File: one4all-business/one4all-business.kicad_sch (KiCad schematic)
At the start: 33 parts, among them J10 T1-4, J11 TN1-4, J12 T5-8, J13 TN5-8

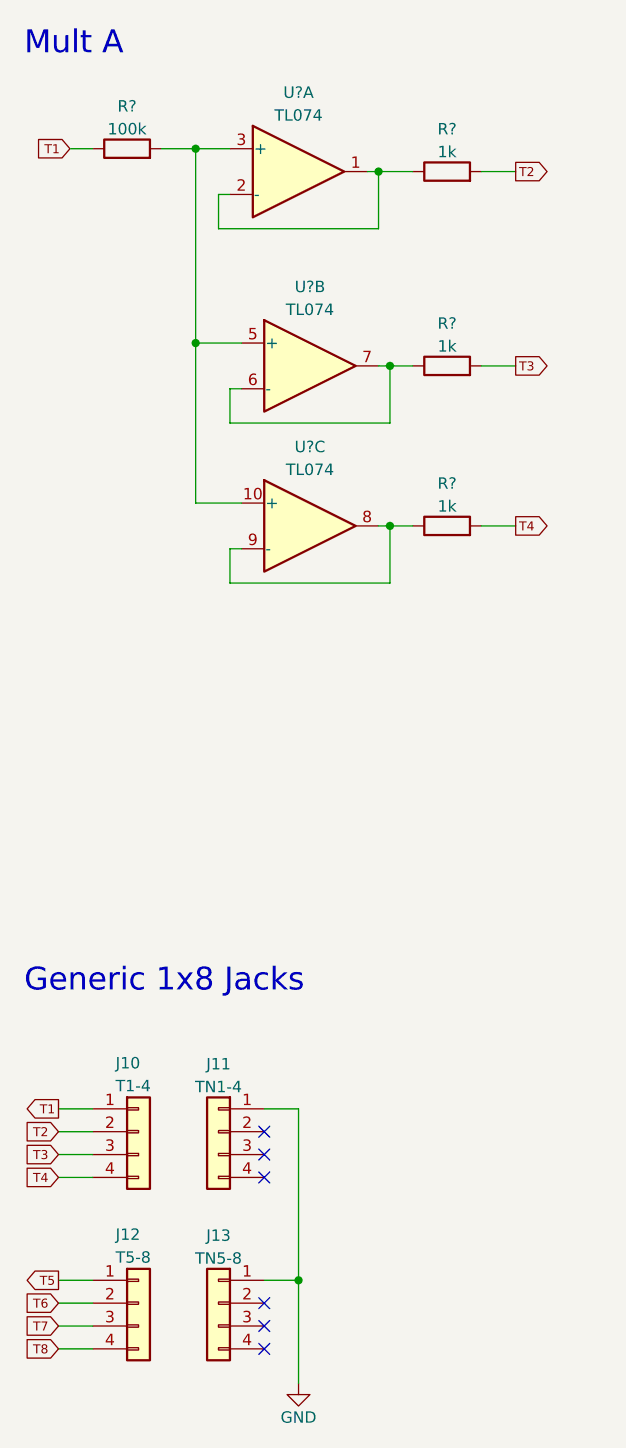
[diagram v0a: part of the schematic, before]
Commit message: :sparkles: one4all register lower buffer to upper buffer
If the lower buffer has no input, it will replicate the upper buffer.
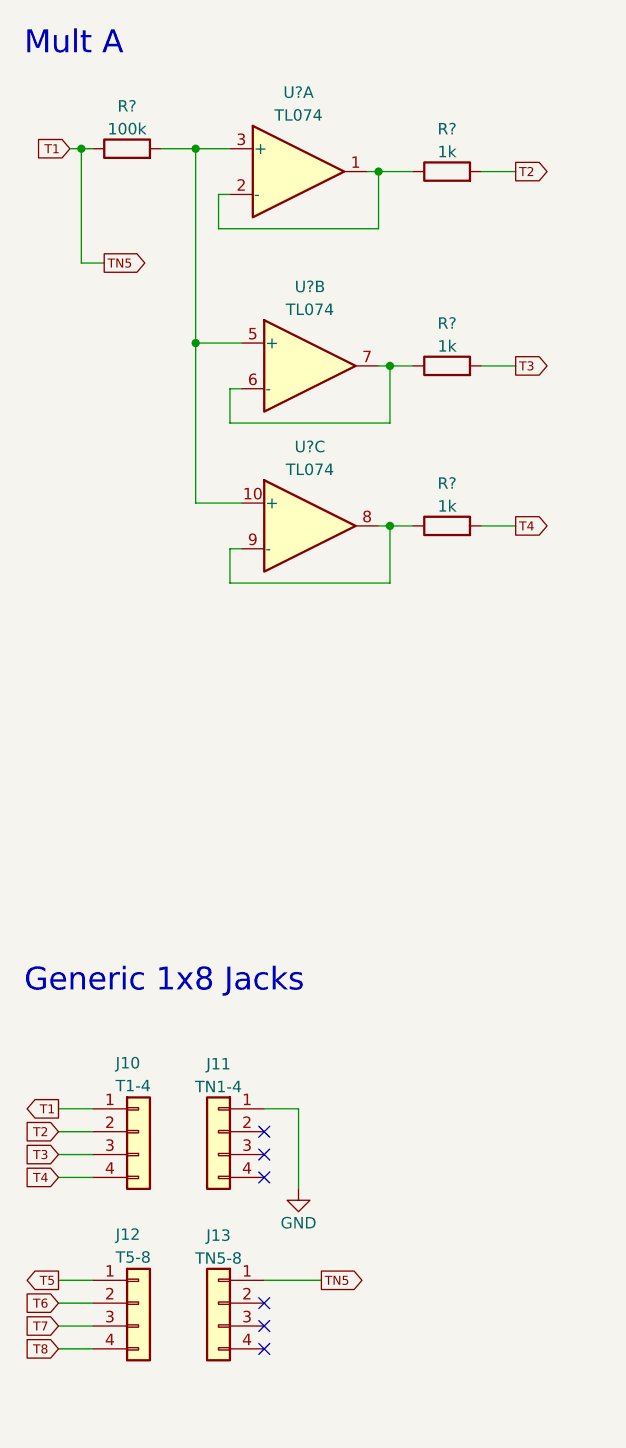
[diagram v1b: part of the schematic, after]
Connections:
- net GND: no longer J13.1 (Pin_1)
- net T1: now also J13.1 (Pin_1)
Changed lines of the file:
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@@
   (junction (at 74.93 85.09) (diameter 0) (color 0 0 0 0)
   )
-  (junction (at 64.77 168.91) (diameter 0) (color 0 0 0 0)
+  (junction (at 40.64 43.18) (diameter 0) (color 0 0 0 0)
   )
   (junction (at 257.81 130.81) (diameter 0) (color 0 0 0 0)
@@
     (stroke (width 0) (type default) (color 0 0 0 0))
   )
-  (wire (pts (xy 39.37 43.18) (xy 41.91 43.18))
+  (wire (pts (xy 39.37 43.18) (xy 40.64 43.18))
     (stroke (width 0) (type default) (color 0 0 0 0))
   )
@@
     (stroke (width 0) (type default) (color 0 0 0 0))
   )
+  (wire (pts (xy 40.64 43.18) (xy 41.91 43.18))
+    (stroke (width 0) (type default) (color 0 0 0 0))
+  )
   (wire (pts (xy 212.09 146.05) (xy 214.63 146.05))
     (stroke (width 0) (type default) (color 0 0 0 0))
@@
     (stroke (width 0) (type default) (color 0 0 0 0))
   )
-  (wire (pts (xy 60.96 168.91) (xy 64.77 168.91))
-    (stroke (width 0) (type default) (color 0 0 0 0))
-  )
   (wire (pts (xy 134.62 64.77) (xy 134.62 82.55))
     (stroke (width 0) (type default) (color 0 0 0 0))
@@
     (stroke (width 0) (type default) (color 0 0 0 0))
   )
+  (wire (pts (xy 40.64 55.88) (xy 40.64 43.18))
+    (stroke (width 0) (type default) (color 0 0 0 0))
+  )
   (wire (pts (xy 257.81 138.43) (xy 273.05 138.43))
     (stroke (width 0) (type default) (color 0 0 0 0))
@@
     (stroke (width 0) (type default) (color 0 0 0 0))
   )
+  (wire (pts (xy 60.96 168.91) (xy 67.31 168.91))
+    (stroke (width 0) (type default) (color 0 0 0 0))
+  )
   (wire (pts (xy 154.94 45.72) (xy 156.21 45.72))
     (stroke (width 0) (type default) (color 0 0 0 0))
@@
     (stroke (width 0) (type default) (color 0 0 0 0))
   )
+  (wire (pts (xy 43.18 55.88) (xy 40.64 55.88))
+    (stroke (width 0) (type default) (color 0 0 0 0))
+  )
   (wire (pts (xy 167.64 135.89) (xy 167.64 138.43))
     (stroke (width 0) (type default) (color 0 0 0 0))
@@
     (stroke (width 0) (type default) (color 0 0 0 0))
   )
-  (wire (pts (xy 64.77 168.91) (xy 64.77 180.34))
+  (wire (pts (xy 64.77 149.86) (xy 64.77 158.75))
     (stroke (width 0) (type default) (color 0 0 0 0))
   )
   (wire (pts (xy 187.96 130.81) (xy 182.88 130.81))
-    (stroke (width 0) (type default) (color 0 0 0 0))
-  )
-  (wire (pts (xy 64.77 149.86) (xy 64.77 168.91))
     (stroke (width 0) (type default) (color 0 0 0 0))
   )
@@
     )
   )
+  (global_label "TN5" (shape output) (at 67.31 168.91 0) (fields_autoplaced)
+    (effects (font (size 1 1)) (justify left))
+    (property "Intersheet References" "${INTERSHEET_REFS}" (id 0) (at 71.9719 168.8475 0)
+      (effects (font (size 1 1)) (justify left) hide)
+    )
+  )
   (global_label "T7" (shape input) (at 38.1 173.99 180) (fields_autoplaced)
     (effects (font (size 1 1)) (justify right))
@@
     (effects (font (size 1 1)) (justify left))
     (property "Intersheet References" "${INTERSHEET_REFS}" (id 0) (at 92.5143 45.6575 0)
+      (effects (font (size 1 1)) (justify left) hide)
+    )
+  )
+  (global_label "TN5" (shape output) (at 43.18 55.88 0) (fields_autoplaced)
+    (effects (font (size 1 1)) (justify left))
+    (property "Intersheet References" "${INTERSHEET_REFS}" (id 0) (at 47.8419 55.8175 0)
       (effects (font (size 1 1)) (justify left) hide)
     )
@@
     (pin "2")
   )
-  (symbol (lib_id "power:GND") (at 64.77 180.34 0) (unit 1)
+  (symbol (lib_id "power:GND") (at 64.77 158.75 0) (unit 1)
     (in_bom yes) (on_board yes)
-    (property "Reference" "#PWR?" (id 0) (at 64.77 186.69 0)
-      (effects (font (size 1.27 1.27)) hide)
-    )
-    (property "Value" "GND" (id 1) (at 64.77 184.15 0))
-    (property "Footprint" "" (id 2) (at 64.77 180.34 0)
-      (effects (font (size 1.27 1.27)) hide)
-    )
-    (property "Datasheet" "" (id 3) (at 64.77 180.34 0)
-      (effects (font (size 1.27 1.27)) hide)
-    )
+    (property "Reference" "#PWR?" (id 0) (at 64.77 165.1 0)
+      (effects (font (size 1.27 1.27)) hide)
+    )
+    (property "Value" "GND" (id 1) (at 64.77 162.56 0))
+    (property "Footprint" "" (id 2) (at 64.77 158.75 0)
+      (effects (font (size 1.27 1.27)) hide)
+    )
+    (property "Datasheet" "" (id 3) (at 64.77 158.75 0)
+      (effects (font (size 1.27 1.27)) hide)
+    )
